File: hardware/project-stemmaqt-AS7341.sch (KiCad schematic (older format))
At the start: 21 parts, among them J1 SM04B-SRSS-TB(LF)(SN), J2 SM04B-SRSS-TB(LF)(SN), J3 Conn_01x03_Male, Q1 Q_PMOS_GSD, U1 DS2482S-100+

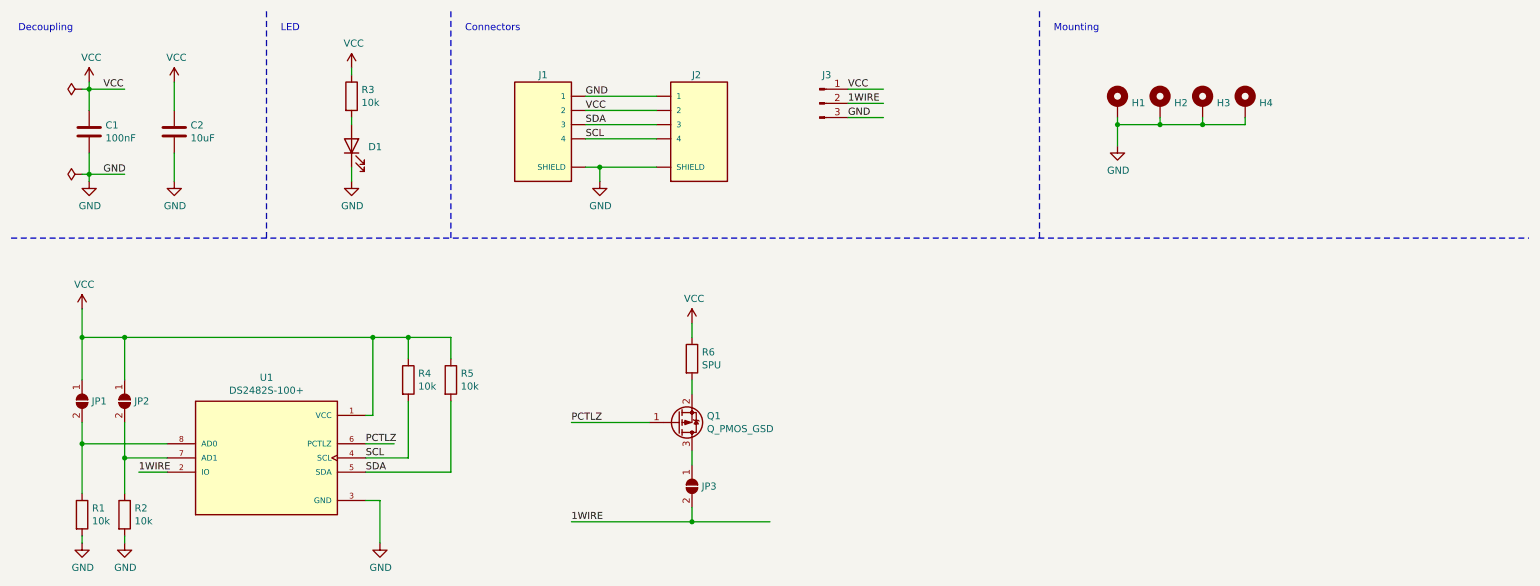
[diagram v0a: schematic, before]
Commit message: Update schematic for AS7341
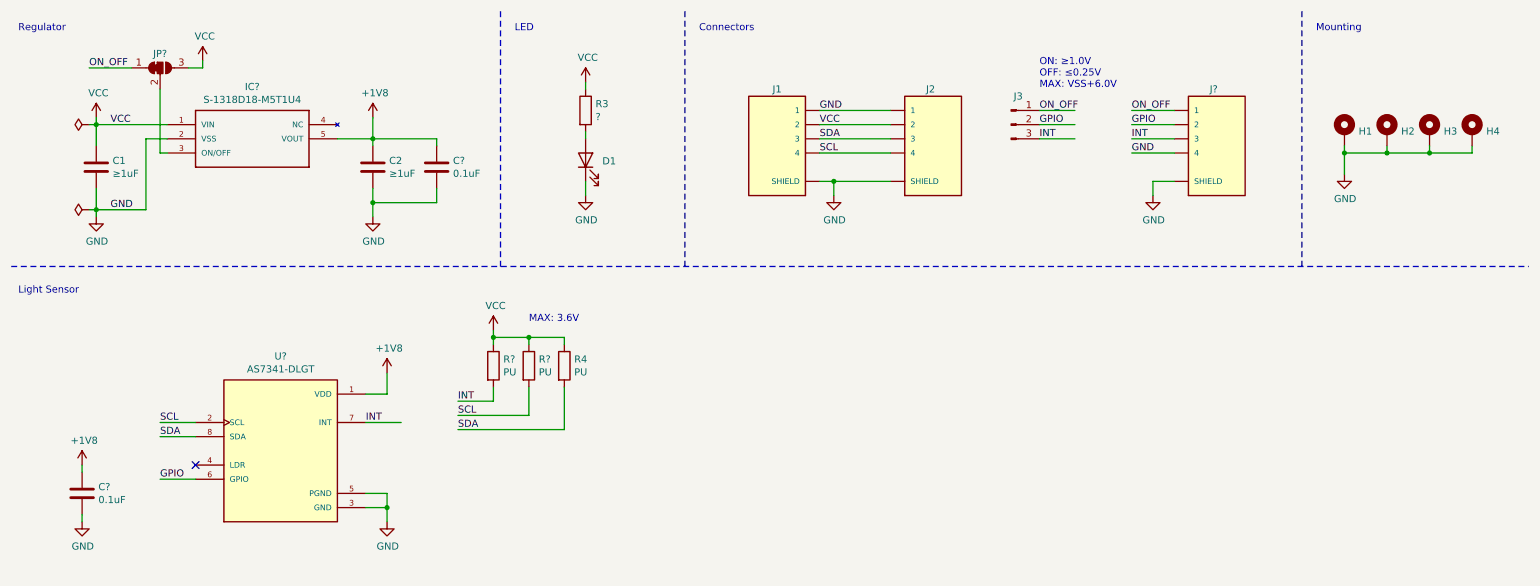
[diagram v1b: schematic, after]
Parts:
- removed JP1: AD0, Jumper:SolderJumper-2_P1.3mm_Open_RoundedPad1.0x1.5mm, symbol Jumper:SolderJumper_2_Open
- removed JP2: AD1, Jumper:SolderJumper-2_P1.3mm_Open_RoundedPad1.0x1.5mm, symbol Jumper:SolderJumper_2_Open
- removed JP3: SPU, Jumper:SolderJumper-2_P1.3mm_Open_RoundedPad1.0x1.5mm, symbol Jumper:SolderJumper_2_Open
- removed Q1: Q_PMOS_GSD, Package_TO_SOT_SMD:SOT-23, symbol Device:Q_PMOS_GSD
- removed R1, R2, R5: 10k, Resistor_SMD:R_0603_1608Metric, symbol Device:R
- removed R6: SPU, Resistor_SMD:R_0603_1608Metric, symbol Device:R
- removed U1: DS2482S-100+, SOIC127P600X175-8N, symbol DS2482S-100_:DS2482S-100+
- added C? (x2): 0.1uF, Capacitor_SMD:C_0603_1608Metric, symbol Device:C
- added IC?: S-1318D18-M5T1U4, SOT95P275X130-5N, symbol S-1318D18-M5T1U4:S-1318D18-M5T1U4
- added J?: SM04B-SRSS-TB(LF)(SN), JST_SM04B-SRSS-TB(LF)(SN), symbol SM04B-SRSS-TB_LF__SN_:SM04B-SRSS-TB(LF)(SN)
- added JP?: SolderJumper_3_Bridged12, symbol Jumper:SolderJumper_3_Bridged12
- added R? (x2): PU, Resistor_SMD:R_0603_1608Metric, symbol Device:R
- added U?: AS7341-DLGT, PSON80P310X200X110-8N, symbol AS7341-DLGT:AS7341-DLGT
- C1: value 100nF -> ≥1uF; footprint Capacitor_SMD:C_0603_1608Metric -> Capacitor_SMD:C_0805_2012Metric
- C2: value 10uF -> ≥1uF; footprint Capacitor_SMD:C_1210_3225Metric -> Capacitor_SMD:C_0805_2012Metric
- R3: value 10k -> ?
- R4: value 10k -> PU
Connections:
- net labels added: +1V8, GPIO, INT, ON_OFF
- net labels removed: 1WIRE, PCTLZ
- wire segments 65 -> 75
- no-connect marks 0 -> 1
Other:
- note added: "Light Sensor"
- note added: "MAX: 3.6V"
- note added: "ON: ≥1.0V\nOFF: ≤0.25V\nMAX: VSS+6.0V"
- note added: "Regulator"
- note removed: "Decoupling"
- moved on the sheet: C1, C2, D1, H1, H2, H3, H4, J1, J2, J3, R3, R4

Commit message: Change regulator to TPS7A0218PDBVR
Although use TPS7A0233PDBVR symbol and footprint.
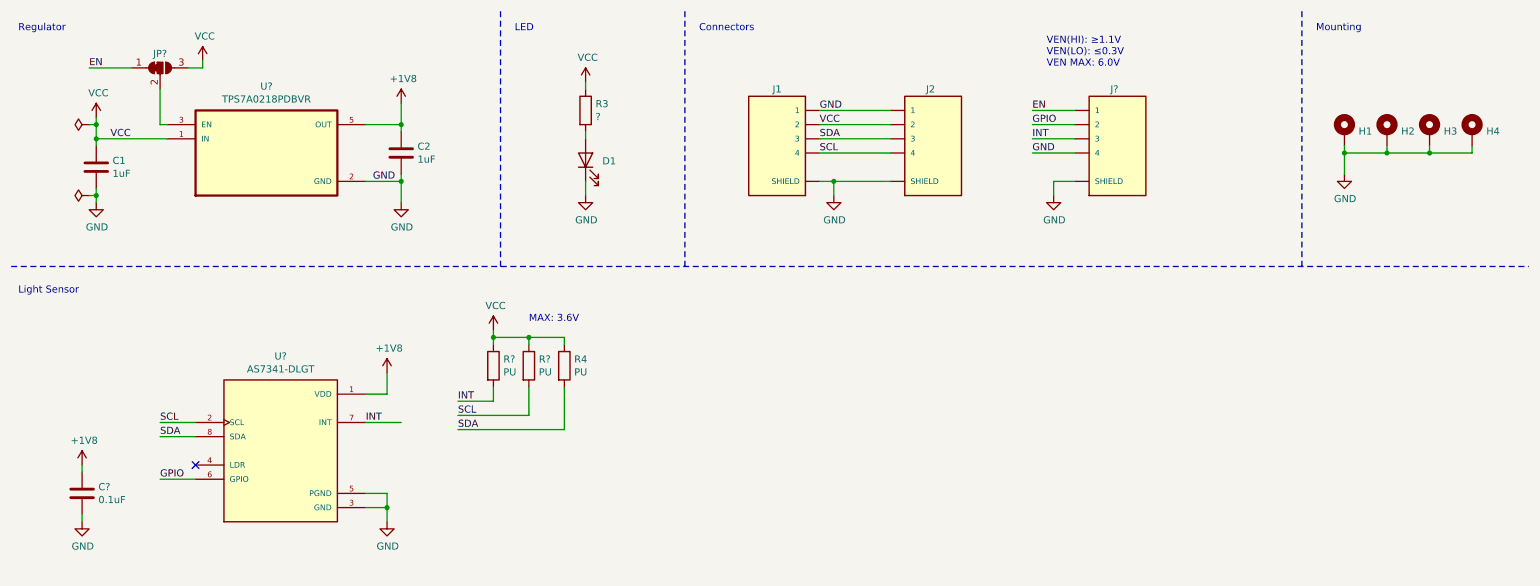
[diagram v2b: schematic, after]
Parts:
- removed C?: 0.1uF, Capacitor_SMD:C_0603_1608Metric, symbol Device:C
- removed IC?: S-1318D18-M5T1U4, SOT95P275X130-5N, symbol S-1318D18-M5T1U4:S-1318D18-M5T1U4
- removed J3: Conn_01x03_Male, Connector_PinHeader_2.54mm:PinHeader_1x03_P2.54mm_Vertical, symbol Connector:Conn_01x03_Male
- added U?: TPS7A0218PDBVR, SOT95P280X145-5N, symbol TPS7A0233PDBVR:TPS7A0233PDBVR
- C1, C2: value ≥1uF -> 1uF
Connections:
- net labels added: EN
- net labels removed: ON_OFF
- wire segments 75 -> 67
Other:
- note added: "VEN(HI): ≥1.1V\nVEN(LO): ≤0.3V\nVEN MAX: 6.0V"
- note removed: "ON: ≥1.0V\nOFF: ≤0.25V\nMAX: VSS+6.0V"
- moved on the sheet: C2, J?
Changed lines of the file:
@@
-	1    0    0    -1
-$EndComp
-Text Label 7750 1200 0    50   ~ 0
-ON_OFF
-Text Label 7750 1300 0    50   ~ 0
-GPIO
-Text Label 7750 1400 0    50   ~ 0
-INT
-Wire Wire Line
-	8000 1400 7750 1400
-Wire Wire Line
-	8000 1300 7750 1300
-Wire Wire Line
-	8000 1200 7750 1200
-$Comp
-L Connector:Conn_01x03_Male J3
-U 1 1 613DEF1D
-P 7550 1300
-F 0 "J3" H 7600 1500 50  0000 C CNN
-F 1 "Conn_01x03_Male" H 7658 1490 50  0001 C CNN
-F 2 "Connector_PinHeader_2.54mm:PinHeader_1x03_P2.54mm_Vertical" H 7550 1300 50  0001 C CNN
-F 3 "~" H 7550 1300 50  0001 C CNN
-	1    7550 1300
 	1    0    0    -1
 $EndComp
@@
 L Device:C C2
 U 1 1 6145671A
-P 3050 1600
-F 0 "C2" H 3165 1646 50  0000 L CNN
-F 1 "≥1uF" H 3165 1555 50  0000 L CNN
-F 2 "Capacitor_SMD:C_0805_2012Metric" H 3050 1600 50  0001 C CNN
-F 3 "~" H 3050 1600 50  0001 C CNN
-	1    3050 1600
+P 3250 1500
+F 0 "C2" H 3365 1546 50  0000 L CNN
+F 1 "1uF" H 3365 1455 50  0000 L CNN
+F 2 "Capacitor_SMD:C_0805_2012Metric" H 3250 1500 50  0001 C CNN
+F 3 "~" H 3250 1500 50  0001 C CNN
+	1    3250 1500
 	1    0    0    -1
 $EndComp
@@
 L power:GND #PWR06
 U 1 1 61456726
-P 3050 1950
-F 0 "#PWR06" H 3050 1700 50  0001 C CNN
-F 1 "GND" H 3055 1777 50  0000 C CNN
-F 2 "" H 3050 1950 50  0001 C CNN
-F 3 "" H 3050 1950 50  0001 C CNN
-	1    3050 1950
-	1    0    0    -1
-$EndComp
-Wire Wire Line
-	3050 1250 3050 1400
-Wire Wire Line
-	3050 1750 3050 1850
+P 3250 1850
+F 0 "#PWR06" H 3250 1600 50  0001 C CNN
+F 1 "GND" H 3255 1677 50  0000 C CNN
+F 2 "" H 3250 1850 50  0001 C CNN
+F 3 "" H 3250 1850 50  0001 C CNN
+	1    3250 1850
+	1    0    0    -1
+$EndComp
+Wire Wire Line
+	3250 1150 3250 1300
 Text Notes 4050 650  0    50   ~ 0
 LED
@@
 L SM04B-SRSS-TB_LF__SN_:SM04B-SRSS-TB(LF)(SN) J?
 U 1 1 6248E788
-P 9000 1400
-F 0 "J?" H 8950 1750 50  0000 L CNN
-F 1 "SM04B-SRSS-TB(LF)(SN)" H 8943 924 50  0001 C CNN
-F 2 "JST_SM04B-SRSS-TB(LF)(SN)" H 9000 1400 50  0001 L BNN
-F 3 "" H 9000 1400 50  0001 L BNN
-F 4 "Manufacturer recommendations" H 9000 1400 50  0001 L BNN "STANDARD"
-F 5 "JST" H 9000 1400 50  0001 L BNN "MANUFACTURER"
-	1    9000 1400
-	1    0    0    -1
-$EndComp
-Wire Wire Line
-	8400 1500 8700 1500
-Wire Wire Line
-	8700 1400 8400 1400
-Wire Wire Line
-	8400 1300 8700 1300
-Wire Wire Line
-	8400 1200 8700 1200
-Wire Wire Line
-	8550 1800 8550 1700
+P 8300 1400
+F 0 "J?" H 8250 1750 50  0000 L CNN
+F 1 "SM04B-SRSS-TB(LF)(SN)" H 8243 924 50  0001 C CNN
+F 2 "JST_SM04B-SRSS-TB(LF)(SN)" H 8300 1400 50  0001 L BNN
+F 3 "" H 8300 1400 50  0001 L BNN
+F 4 "Manufacturer recommendations" H 8300 1400 50  0001 L BNN "STANDARD"
+F 5 "JST" H 8300 1400 50  0001 L BNN "MANUFACTURER"
+	1    8300 1400
+	1    0    0    -1
+$EndComp
+Wire Wire Line
+	7700 1500 8000 1500
+Wire Wire Line
+	8000 1400 7700 1400
+Wire Wire Line
+	7700 1300 8000 1300
+Wire Wire Line
+	7700 1200 8000 1200
+Wire Wire Line
+	7850 1800 7850 1700
 $Comp
 L power:GND #PWR?
 U 1 1 6249B040
-P 8550 1800
-F 0 "#PWR?" H 8550 1550 50  0001 C CNN
-F 1 "GND" H 8555 1627 50  0000 C CNN
-F 2 "" H 8550 1800 50  0001 C CNN
-F 3 "" H 8550 1800 50  0001 C CNN
-	1    8550 1800
-	1    0    0    -1
-$EndComp
-Wire Wire Line
-	8700 1700 8550 1700
-Text Label 8400 1500 0    50   ~ 0
+P 7850 1800
+F 0 "#PWR?" H 7850 1550 50  0001 C CNN
+F 1 "GND" H 7855 1627 50  0000 C CNN
+F 2 "" H 7850 1800 50  0001 C CNN
+F 3 "" H 7850 1800 50  0001 C CNN
+	1    7850 1800
+	1    0    0    -1
+$EndComp
+Wire Wire Line
+	8000 1700 7850 1700
+Text Label 7700 1500 0    50   ~ 0
 GND
-Text Label 8400 1400 0    50   ~ 0
+Text Label 7700 1400 0    50   ~ 0
 INT
-Text Label 8400 1300 0    50   ~ 0
+Text Label 7700 1300 0    50   ~ 0
 GPIO
-Text Label 8400 1200 0    50   ~ 0
-ON_OFF
+Text Label 7700 1200 0    50   ~ 0
+EN
 $Comp
 L AS7341-DLGT:AS7341-DLGT U?
@@
 $EndComp
 $Comp
-L S-1318D18-M5T1U4:S-1318D18-M5T1U4 IC?
-U 1 1 624CCF5F
-P 1600 1300
-F 0 "IC?" H 2200 1567 50  0000 C CNN
-F 1 "S-1318D18-M5T1U4" H 2200 1476 50  0000 C CNN
-F 2 "SOT95P275X130-5N" H 1600 1300 50  0001 L BNN
-F 3 "" H 1600 1300 50  0001 L BNN
-F 4 "ABLIC U.S.A. Inc." H 1600 1300 50  0001 L BNN "Manufacturer_Name"
-F 5 "S-1318D18-M5T1U4" H 1600 1300 50  0001 L BNN "Manufacturer_Part_Number"
-F 6 "LDO Voltage Regulators 100MA VOLT REG ULTRA LOW IQ" H 1600 1300 50  0001 L BNN "Description"
-F 7 "" H 1600 1300 50  0001 L BNN "RS_Price-Stock"
-F 8 "" H 1600 1300 50  0001 L BNN "RS_Part_Number"
-F 9 "1.3mm" H 1600 1300 50  0001 L BNN "Height"
-	1    1600 1300
-	1    0    0    -1
-$EndComp
-$Comp
 L Jumper:SolderJumper_3_Bridged12 JP?
 U 1 1 624D6D20
@@
 	1050 900  1350 900
 Text Label 1050 900  0    50   ~ 0
-ON_OFF
-Wire Wire Line
-	1100 1750 1100 1900
-Wire Wire Line
-	1100 1300 1100 1450
-Text Label 1200 1900 0    50   ~ 0
+EN
+Wire Wire Line
+	1100 1750 1100 1800
+Wire Wire Line
+	1100 1300 1100 1400
+Text Label 3050 1700 0    50   ~ 0
 GND
-Text Label 1200 1300 0    50   ~ 0
+Text Label 1200 1400 0    50   ~ 0
 VCC
 Wire Wire Line
-	1100 1900 1100 1950
-Connection ~ 1100 1900
-Wire Wire Line
-	1050 1900 1100 1900
+	1100 1800 1100 1850
+Connection ~ 1100 1800
+Wire Wire Line
+	1050 1800 1100 1800
 $Comp
 L power:PWR_FLAG #FLG0102
 U 1 1 61367C22
-P 1050 1900
-F 0 "#FLG0102" H 1050 1975 50  0001 C CNN
-F 1 "PWR_FLAG" V 1050 2027 50  0001 L CNN
-F 2 "" H 1050 1900 50  0001 C CNN
-F 3 "~" H 1050 1900 50  0001 C CNN
-	1    1050 1900
+P 1050 1800
+F 0 "#FLG0102" H 1050 1875 50  0001 C CNN
+F 1 "PWR_FLAG" V 1050 1927 50  0001 L CNN
+F 2 "" H 1050 1800 50  0001 C CNN
+F 3 "~" H 1050 1800 50  0001 C CNN
+	1    1050 1800
 	0    -1   -1   0
 $EndComp
@@
 L power:GND #PWR0106
 U 1 1 61315B55
-P 1100 1950
-F 0 "#PWR0106" H 1100 1700 50  0001 C CNN
-F 1 "GND" H 1105 1777 50  0000 C CNN
-F 2 "" H 1100 1950 50  0001 C CNN
-F 3 "" H 1100 1950 50  0001 C CNN
-	1    1100 1950
+P 1100 1850
+F 0 "#PWR0106" H 1100 1600 50  0001 C CNN
+F 1 "GND" H 1105 1677 50  0000 C CNN
+F 2 "" H 1100 1850 50  0001 C CNN
+F 3 "" H 1100 1850 50  0001 C CNN
+	1    1100 1850
 	1    0    0    -1
 $EndComp
@@
 P 1100 1600
 F 0 "C1" H 1215 1646 50  0000 L CNN
-F 1 "≥1uF" H 1215 1555 50  0000 L CNN
+F 1 "1uF" H 1215 1555 50  0000 L CNN
 F 2 "Capacitor_SMD:C_0805_2012Metric" H 1100 1600 50  0001 C CNN
 F 3 "~" H 1100 1600 50  0001 C CNN
@@
 $EndComp
 Wire Wire Line
-	1100 1300 1600 1300
-Wire Wire Line
-	1600 1400 1450 1400
-Wire Wire Line
-	1450 1400 1450 1900
-Wire Wire Line
-	1100 1900 1450 1900
-Wire Wire Line
-	1550 1050 1550 1500
-Wire Wire Line
-	1550 1500 1600 1500
-Wire Wire Line
-	2800 1400 3050 1400
-Connection ~ 3050 1400
-Wire Wire Line
-	3050 1400 3050 1450
+	3000 1300 3250 1300
+Connection ~ 3250 1300
+Wire Wire Line
+	3250 1300 3250 1350
 Text Notes 550  650  0    50   ~ 0
 Regulator
@@
 L power:+1V8 #PWR?
 U 1 1 625BC6EB
-P 3050 1250
-F 0 "#PWR?" H 3050 1100 50  0001 C CNN
-F 1 "+1V8" H 3065 1423 50  0000 C CNN
-F 2 "" H 3050 1250 50  0001 C CNN
-F 3 "" H 3050 1250 50  0001 C CNN
-	1    3050 1250
+P 3250 1150
+F 0 "#PWR?" H 3250 1000 50  0001 C CNN
+F 1 "+1V8" H 3265 1323 50  0000 C CNN
+F 2 "" H 3250 1150 50  0001 C CNN
+F 3 "" H 3250 1150 50  0001 C CNN
+	1    3250 1150
 	1    0    0    -1
 $EndComp
@@
 $Comp
 L Device:C C?
-U 1 1 625DF72E
-P 3500 1600
-F 0 "C?" H 3615 1646 50  0000 L CNN
-F 1 "0.1uF" H 3615 1555 50  0000 L CNN
-F 2 "Capacitor_SMD:C_0603_1608Metric" H 3500 1600 50  0001 C CNN
-F 3 "~" H 3500 1600 50  0001 C CNN
-	1    3500 1600
-	1    0    0    -1
-$EndComp
-Wire Wire Line
-	3050 1400 3500 1400
-Wire Wire Line
-	3500 1400 3500 1450
-Wire Wire Line
-	3500 1750 3500 1850
-Wire Wire Line
-	3500 1850 3050 1850
-Connection ~ 3050 1850
-Wire Wire Line
-	3050 1850 3050 1950
-$Comp
-L Device:C C?
 U 1 1 625EF5BE
 P 1000 3900
@@
 	1    0    0    -1
 $EndComp
-Text Notes 7750 1050 0    50   ~ 0
-ON: ≥1.0V\nOFF: ≤0.25V\nMAX: VSS+6.0V
+Text Notes 7800 900  0    50   ~ 0
+VEN(HI): ≥1.1V\nVEN(LO): ≤0.3V\nVEN MAX: 6.0V
 Text Notes 550  2500 0    50   ~ 0
 Light Sensor
@@
 Text Notes 4150 2700 0    50   ~ 0
 MAX: 3.6V
+$Comp
+L TPS7A0233PDBVR:TPS7A0233PDBVR U?
+U 1 1 626C44EE
+P 2300 1500
+F 0 "U?" H 2300 1970 50  0000 C CNN
+F 1 "TPS7A0218PDBVR" H 2300 1879 50  0000 C CNN
+F 2 "SOT95P280X145-5N" H 2300 1500 50  0001 L BNN
+F 3 "" H 2300 1500 50  0001 L BNN
+	1    2300 1500
+	1    0    0    -1
+$EndComp
+Wire Wire Line
+	3250 1650 3250 1700
+Wire Wire Line
+	1100 1400 1600 1400
+Connection ~ 1100 1400
+Wire Wire Line
+	1100 1400 1100 1450
+Wire Wire Line
+	1600 1300 1550 1300
+Wire Wire Line
+	1550 1300 1550 1050
+Wire Wire Line
+	3000 1700 3250 1700
+Connection ~ 3250 1700
+Wire Wire Line
+	3250 1700 3250 1850
 $EndSCHEMATC

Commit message: First placement
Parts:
- JP1: renamed from JP?; footprint (none) -> Jumper:SolderJumper-3_P1.3mm_Bridged12_RoundedPad1.0x1.5mm
- gave numbers to parts that had none: 6
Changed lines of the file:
@@
 Mounting
 $Comp
-L SM04B-SRSS-TB_LF__SN_:SM04B-SRSS-TB(LF)(SN) J?
+L SM04B-SRSS-TB_LF__SN_:SM04B-SRSS-TB(LF)(SN) J3
 U 1 1 6248E788
 P 8300 1400
-F 0 "J?" H 8250 1750 50  0000 L CNN
+F 0 "J3" H 8250 1750 50  0000 L CNN
 F 1 "SM04B-SRSS-TB(LF)(SN)" H 8243 924 50  0001 C CNN
 F 2 "JST_SM04B-SRSS-TB(LF)(SN)" H 8300 1400 50  0001 L BNN
@@
 	7850 1800 7850 1700
 $Comp
-L power:GND #PWR?
+L power:GND #PWR0101
 U 1 1 6249B040
 P 7850 1800
-F 0 "#PWR?" H 7850 1550 50  0001 C CNN
+F 0 "#PWR0101" H 7850 1550 50  0001 C CNN
 F 1 "GND" H 7855 1627 50  0000 C CNN
 F 2 "" H 7850 1800 50  0001 C CNN
@@
 EN
 $Comp
-L AS7341-DLGT:AS7341-DLGT U?
+L AS7341-DLGT:AS7341-DLGT U2
 U 1 1 624CAA7C
 P 2400 3600
-F 0 "U?" H 2400 4267 50  0000 C CNN
+F 0 "U2" H 2400 4267 50  0000 C CNN
 F 1 "AS7341-DLGT" H 2400 4176 50  0000 C CNN
 F 2 "PSON80P310X200X110-8N" H 2400 3600 50  0001 L BNN
@@
 $EndComp
 $Comp
-L Jumper:SolderJumper_3_Bridged12 JP?
+L Jumper:SolderJumper_3_Bridged12 JP1
 U 1 1 624D6D20
 P 1550 900
-F 0 "JP?" H 1550 1000 50  0000 C CNN
+F 0 "JP1" H 1550 1000 50  0000 C CNN
 F 1 "SolderJumper_3_Bridged12" H 1300 1050 50  0001 C CNN
-F 2 "" H 1550 900 50  0001 C CNN
+F 2 "Jumper:SolderJumper-3_P1.3mm_Bridged12_RoundedPad1.0x1.5mm" H 1550 900 50  0001 C CNN
 F 3 "~" H 1550 900 50  0001 C CNN
 	1    1550 900
@@
 $EndComp
 $Comp
-L power:VCC #PWR?
+L power:VCC #PWR0102
 U 1 1 624ECE5E
 P 1850 850
-F 0 "#PWR?" H 1850 700 50  0001 C CNN
+F 0 "#PWR0102" H 1850 700 50  0001 C CNN
 F 1 "VCC" H 1865 1023 50  0000 C CNN
 F 2 "" H 1850 850 50  0001 C CNN
@@
 Connection ~ 10500 1500
 $Comp
-L power:GND #PWR?
+L power:GND #PWR0103
 U 1 1 625B7351
 P 3150 4100
-F 0 "#PWR?" H 3150 3850 50  0001 C CNN
+F 0 "#PWR0103" H 3150 3850 50  0001 C CNN
 F 1 "GND" H 3155 3927 50  0000 C CNN
 F 2 "" H 3150 4100 50  0001 C CNN
@@
 	3150 4000 3150 4100
 $Comp
-L power:+1V8 #PWR?
+L power:+1V8 #PWR0104
 U 1 1 625BC6EB
 P 3250 1150
-F 0 "#PWR?" H 3250 1000 50  0001 C CNN
+F 0 "#PWR0104" H 3250 1000 50  0001 C CNN
 F 1 "+1V8" H 3265 1323 50  0000 C CNN
 F 2 "" H 3250 1150 50  0001 C CNN
@@
 NoConn ~ 1800 3700
 $Comp
-L Device:R R?
+L Device:R R2
 U 1 1 625DCDA6
 P 4150 3000
-F 0 "R?" H 4220 3046 50  0000 L CNN
+F 0 "R2" H 4220 3046 50  0000 L CNN
 F 1 "PU" H 4220 2955 50  0000 L CNN
 F 2 "Resistor_SMD:R_0603_1608Metric" V 4080 3000 50  0001 C CNN
@@
 $EndComp
 $Comp
-L Device:R R?
+L Device:R R1
 U 1 1 625DD416
 P 3900 3000
-F 0 "R?" H 3970 3046 50  0000 L CNN
+F 0 "R1" H 3970 3046 50  0000 L CNN
 F 1 "PU" H 3970 2955 50  0000 L CNN
 F 2 "Resistor_SMD:R_0603_1608Metric" V 3830 3000 50  0001 C CNN
@@
 $EndComp
 $Comp
-L Device:C C?
+L Device:C C3
 U 1 1 625EF5BE
 P 1000 3900
-F 0 "C?" H 1115 3946 50  0000 L CNN
+F 0 "C3" H 1115 3946 50  0000 L CNN
 F 1 "0.1uF" H 1115 3855 50  0000 L CNN
 F 2 "Capacitor_SMD:C_0603_1608Metric" H 1000 3900 50  0001 C CNN
@@
 	3150 3200 3150 3050
 $Comp
-L power:GND #PWR?
+L power:GND #PWR0107
 U 1 1 6260C741
 P 1000 4100
-F 0 "#PWR?" H 1000 3850 50  0001 C CNN
+F 0 "#PWR0107" H 1000 3850 50  0001 C CNN
 F 1 "GND" H 1005 3927 50  0000 C CNN
 F 2 "" H 1000 4100 50  0001 C CNN
@@
 	1000 4050 1000 4100
 $Comp
-L power:+1V8 #PWR?
+L power:+1V8 #PWR0108
 U 1 1 6260FC76
 P 1000 3700
-F 0 "#PWR?" H 1000 3550 50  0001 C CNN
+F 0 "#PWR0108" H 1000 3550 50  0001 C CNN
 F 1 "+1V8" H 1015 3873 50  0000 C CNN
 F 2 "" H 1000 3700 50  0001 C CNN
@@
 SDA
 $Comp
-L power:+1V8 #PWR?
+L power:+1V8 #PWR0109
 U 1 1 625C0777
 P 3150 3050
-F 0 "#PWR?" H 3150 2900 50  0001 C CNN
+F 0 "#PWR0109" H 3150 2900 50  0001 C CNN
 F 1 "+1V8" H 3165 3223 50  0000 C CNN
 F 2 "" H 3150 3050 50  0001 C CNN
@@
 	3650 3450 4400 3450
 $Comp
-L power:VCC #PWR?
+L power:VCC #PWR0110
 U 1 1 6267357D
 P 3900 2750
-F 0 "#PWR?" H 3900 2600 50  0001 C CNN
+F 0 "#PWR0110" H 3900 2600 50  0001 C CNN
 F 1 "VCC" H 3915 2923 50  0000 C CNN
 F 2 "" H 3900 2750 50  0001 C CNN
@@
 MAX: 3.6V
 $Comp
-L TPS7A0233PDBVR:TPS7A0233PDBVR U?
+L TPS7A0233PDBVR:TPS7A0233PDBVR U1
 U 1 1 626C44EE
 P 2300 1500
-F 0 "U?" H 2300 1970 50  0000 C CNN
+F 0 "U1" H 2300 1970 50  0000 C CNN
 F 1 "TPS7A0218PDBVR" H 2300 1879 50  0000 C CNN
 F 2 "SOT95P280X145-5N" H 2300 1500 50  0001 L BNN
